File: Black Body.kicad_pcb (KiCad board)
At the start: 2 copper layers, 40 x 55.5 mm, 20 parts, among them IC2 MCP96L00T-E_MX, J1 53307-2471, J2 Conn_01x02, J3 Conn_01x03, J4 Conn_02x08_Top_Bottom

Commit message: Revision
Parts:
- added TP1: TestPoint, Connector_PinHeader_2.54mm:PinHeader_1x01_P2.54mm_Vertical, F.Cu at (125.6, 86.0)
- added TP2: TestPoint, Connector_PinHeader_2.54mm:PinHeader_1x01_P2.54mm_Vertical, F.Cu at (130.0, 86.0)
- added TP3: TestPoint, Connector_PinHeader_2.54mm:PinHeader_1x01_P2.54mm_Vertical, F.Cu at (134.2, 86.0)
- added TP4: TestPoint, Connector_PinHeader_2.54mm:PinHeader_1x01_P2.54mm_Vertical, F.Cu at (125.5, 91.5)
- added TP5: TestPoint, Connector_PinHeader_2.54mm:PinHeader_1x01_P2.54mm_Vertical, F.Cu at (130.2, 91.5)
- added TP6: TestPoint, Connector_PinHeader_2.54mm:PinHeader_1x01_P2.54mm_Vertical, F.Cu at (134.2, 91.5)
- added TP7: TestPoint, Connector_PinHeader_2.54mm:PinHeader_1x01_P2.54mm_Vertical, F.Cu at (125.2, 96.8)
- added TP8: TestPoint, Connector_PinHeader_2.54mm:PinHeader_1x01_P2.54mm_Vertical, F.Cu at (129.2, 96.8)
- C2, C3: footprint Capacitor_SMD:C_0603_1608Metric_Pad1.08x0.95mm_HandSolder -> Capacitor_SMD:C_0805_2012Metric_Pad1.18x1.45mm_HandSolder
- moved J2 0.50 mm to (109.5, 80.0)
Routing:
- net Net-(IC2-SCL): track 16.1 -> 30.1 mm, vias 1 -> 3
- net Net-(IC2-SDA): track 17.6 -> 30.6 mm, vias 1 -> 3
- net Net-(J1-ADC1_IN7): track 20.8 -> 32.7 mm
- net +3V3: track 31.4 -> 41.1 mm
- net GND: vias 3 -> 31
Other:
- board text added: "Kell wuz here"

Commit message: Updated Layout
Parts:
- removed D1, D2, D3, D4: 3V3, Diode_SMD:D_0603_1608Metric_Pad1.05x0.95mm_HandSolder
- removed TP1, TP2, TP3, TP4, TP5, TP6, TP7, TP8: TestPoint, Connector_PinHeader_2.54mm:PinHeader_1x01_P2.54mm_Vertical
- added DB_1: LED, LED_SMD:LED_0603_1608Metric_Pad1.05x0.95mm_HandSolder, F.Cu at (94.2, 94.2)
- added DB_2: LED, LED_SMD:LED_0603_1608Metric_Pad1.05x0.95mm_HandSolder, F.Cu at (98.5, 94.2)
- added DB_3: LED, LED_SMD:LED_0603_1608Metric_Pad1.05x0.95mm_HandSolder, F.Cu at (103.1, 94.2)
- added GND1: TestPoint, Connector_PinHeader_2.54mm:PinHeader_1x01_P2.54mm_Vertical, F.Cu at (119.0, 69.0)
- added GND2: TestPoint, Connector_PinHeader_2.54mm:PinHeader_1x01_P2.54mm_Vertical, F.Cu at (114.0, 69.0)
- added Heartbeat1: LED, LED_SMD:LED_0603_1608Metric_Pad1.05x0.95mm_HandSolder, F.Cu at (112.4, 105.5)
- added INT1: TestPoint, Connector_PinHeader_2.54mm:PinHeader_1x01_P2.54mm_Vertical, F.Cu at (120.2, 115.5)
- added IS_SCL1: TestPoint, Connector_PinHeader_2.54mm:PinHeader_1x01_P2.54mm_Vertical, F.Cu at (124.0, 110.8)
- added IS_SDA1: TestPoint, Connector_PinHeader_2.54mm:PinHeader_1x01_P2.54mm_Vertical, F.Cu at (119.8, 110.8)
- added J5: Conn_01x06, Connector_Molex:Molex_Nano-Fit_105313-xx06_1x06_P2.50mm_Horizontal, F.Cu at (131.9, 104.0)
- added R1: 10k, Resistor_SMD:R_0805_2012Metric, F.Cu at (121.6, 102.0)
- added R10: R, Resistor_SMD:R_0603_1608Metric_Pad0.98x0.95mm_HandSolder, F.Cu at (102.8, 92.2)
- added R2: 1.5k, Resistor_SMD:R_0805_2012Metric, F.Cu at (124.6, 102.0)
- added R3: 1.5k, Resistor_SMD:R_0805_2012Metric, F.Cu at (127.6, 101.9)
- added R9: R, Resistor_SMD:R_0603_1608Metric_Pad0.98x0.95mm_HandSolder, F.Cu at (118.5, 104.7)
- added TP_SCL1: LED, LED_SMD:LED_0603_1608Metric_Pad1.05x0.95mm_HandSolder, F.Cu at (118.6, 106.7)
- added TP_TC_1: TestPoint, Connector_PinHeader_2.54mm:PinHeader_1x01_P2.54mm_Vertical, F.Cu at (93.8, 109.5)
- added TP_TC_2: TestPoint, Connector_PinHeader_2.54mm:PinHeader_1x01_P2.54mm_Vertical, F.Cu at (93.8, 100.5)
- added TP_TC_F_1: TestPoint, Connector_PinHeader_2.54mm:PinHeader_1x01_P2.54mm_Vertical, F.Cu at (98.5, 109.2)
- added TP_TC_F_2: TestPoint, Connector_PinHeader_2.54mm:PinHeader_1x01_P2.54mm_Vertical, F.Cu at (98.8, 100.5)
- added VCC1: TestPoint, Connector_PinHeader_2.54mm:PinHeader_1x01_P2.54mm_Vertical, F.Cu at (115.5, 111.0)
- J3: value Conn_01x03 -> Conn_01x03_Pin
- J4: footprint MX150:CONN_SD-75900-001_2X08_MOL -> UTSVT_Connectors:CONN_SD-75900-001_2X08_MOL
- R4: value 1M -> R
- R7, R8: value 2M -> R
- moved J1 48.5 mm to (111.0, 117.0), turned to 0 degrees
- moved R6 33.5 mm to (97.8, 103.5)
- moved FB2 33.2 mm to (93.8, 103.5), turned to 0 degrees
- moved J2 32.4 mm to (89.5, 105.5)
- moved IC2 32.3 mm to (105.5, 106.5), turned to -90 degrees
- moved FB1 30.3 mm to (93.8, 105.5)
- moved C3 29.8 mm to (100.8, 104.5)
- moved Rb1 28.9 mm to (107.0, 99.8), turned to 0 degrees
- moved R5 28.5 mm to (97.8, 105.5), turned to 180 degrees
- moved J4 24.5 mm to (85.6, 84.2)
- moved Ra1 24.2 mm to (107.0, 97.8), turned to 180 degrees
- moved R4 23.3 mm to (94.3, 92.2), turned to 180 degrees
- moved C2 23.2 mm to (103.0, 98.8), turned to 90 degrees
- moved R7 21.7 mm to (98.4, 92.2)
- moved R8 16.8 mm to (112.4, 103.5)
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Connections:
- net Net-(J1-ADC1_IN7) renamed /INT
- C2 pad 1: +3V3 -> GND
- C2 pad 2: GND -> +3V3
- FB1 pad 2: Net-(D1-A) -> Net-(FB1-Pad2)
- FB2 pad 2: Net-(D2-A) -> Net-(FB2-Pad2)
- IC2 pad 11: unconnected-(IC2-ALERT_1-Pad11) -> /Alert_1
- IC2 pad 12: unconnected-(IC2-ALERT_2-Pad12) -> /Alert_2
- IC2 pad 14: unconnected-(IC2-ALERT_3-Pad14) -> /Alert_3
- IC2 pad 15: unconnected-(IC2-ALERT_4-Pad15) -> /Alert_4
- IC2 pad 19: Net-(IC2-SCL) -> /I2C1_SCL
- IC2 pad 20: Net-(IC2-SDA) -> /I2C1_SDA
- IC2 pad 8: +3V3 -> GND
- J1 pad 12: unconnected-(J1-SPI2_NSS-Pad12) -> /Alert_1
- J1 pad 14: unconnected-(J1-SPI2_MISO-Pad14) -> /Alert_4
- J1 pad 16: unconnected-(J1-SPI2_MOSI-Pad16) -> /Alert_3
- J1 pad 17: unconnected-(J1-SPI1_MOSI-Pad17) -> /DB_Conn_2
- J1 pad 18: unconnected-(J1-SPI2_SCK-Pad18) -> /Alert_2
- J1 pad 19: unconnected-(J1-SPI1_NSS-Pad19) -> /Heartbeat
- J1 pad 20: Net-(J1-CAN_L) -> /CAN_L
- J1 pad 21: unconnected-(J1-SPI1_MISO-Pad21) -> /DB_Conn_3
- J1 pad 22: Net-(J1-CAN_H) -> /CAN_H
- J1 pad 23: unconnected-(J1-SPI1_SCK-Pad23) -> /DB_Conn_1
- J1 pad 24: Net-(J1-+24V_In) -> +24V
- J1 pad 4: Net-(IC2-SDA) -> /I2C1_SDA
- J1 pad 6: Net-(IC2-SCL) -> /I2C1_SCL
- J3 pad 1: Net-(IC2-SCL) -> /I2C1_SDA
- J3 pad 2: Net-(IC2-SDA) -> /I2C1_SCL
- J4 pad 1: Net-(J1-+24V_In) -> +24V
- J4 pad 12: unconnected-(J4-Pin_12-Pad12) -> /CAN_L
- J4 pad 13: unconnected-(J4-Pin_13-Pad13) -> /CAN_H
- J4 pad 5: Net-(J1-CAN_H) -> /CAN_H
- J4 pad 6: Net-(J1-CAN_L) -> /CAN_L
- J4 pad 8: unconnected-(J4-Pin_8-Pad8) -> GND
- J4 pad 9: unconnected-(J4-Pin_9-Pad9) -> +24V
- R4 pad 1: Net-(D2-A) -> Net-(DB_1-A)
- R5 pad 2: Net-(D1-A) -> Net-(FB1-Pad2)
- R6 pad 2: Net-(D2-A) -> Net-(FB2-Pad2)
- R7 pad 1: GND -> Net-(DB_2-A)
- R7 pad 2: Net-(D1-A) -> +3V3
- R8 pad 1: GND -> Net-(Heartbeat1-A)
- R8 pad 2: Net-(D2-A) -> +3V3
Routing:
- net /I2C1_SCL: track 0.00 -> 80.2 mm, vias 0 -> 1
- net /I2C1_SDA: track 0.00 -> 68.2 mm, vias 0 -> 2
- net /CAN_L: track 0.00 -> 53.4 mm, vias 0 -> 3
- net /CAN_H: track 0.00 -> 48.0 mm, vias 0 -> 3
- net +3V3: track 41.1 -> 3.10 mm, vias 3 -> 0
- net Net-(J1-CAN_L): track 33.8 -> 0.00 mm
- net /DB_Conn_1: track 0.00 -> 30.7 mm, vias 0 -> 1
- net /DB_Conn_2: track 0.00 -> 30.7 mm, vias 0 -> 3
- net Net-(IC2-SDA): track 30.6 -> 0.00 mm, vias 3 -> 0
- net Net-(IC2-SCL): track 30.1 -> 0.00 mm, vias 3 -> 0
- net Net-(J1-CAN_H): track 29.6 -> 0.00 mm, vias 1 -> 0
- net Net-(D2-A): track 29.5 -> 0.00 mm, vias 3 -> 0
- net /INT: track 32.7 -> 60.5 mm, vias 0 -> 2
- net /DB_Conn_3: track 0.00 -> 27.4 mm, vias 0 -> 1
- net Net-(J1-+24V_In): track 24.1 -> 0.00 mm, vias 2 -> 0
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- added copper zone on F.Cu, net +24V
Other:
- board outline removed
- board text removed: "Kell wuz here"

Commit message: connector update
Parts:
- moved GND1 23.8 mm to (113.8, 92.2)
- moved GND2 23.8 mm to (108.8, 92.2)
- moved INT1 2.75 mm to (120.2, 118.2)
- moved TP_TC_F_2 0.75 mm to (98.8, 99.8)
- moved TP_TC_2 0.40 mm to (93.5, 100.2)
- moved J2 0.31 mm to (89.1, 105.5)
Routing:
- net +3V3: track 3.10 -> 71.9 mm, vias 0 -> 3
- net +24V: track 0.00 -> 38.6 mm, vias 0 -> 2
- net /I2C1_SCL: track 80.2 -> 75.8 mm, vias 1 -> 2
- net /INT: track 60.5 -> 62.6 mm
- net Net-(J2-Pin_2): track 7.05 -> 8.41 mm
- net Net-(IC2-VIN+): track 11.6 -> 12.4 mm
- net /DB_Conn_2: vias 3 -> 4
- removed copper zone on F.Cu, net +24V
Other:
- board outline added: 78.8 x 58 mm
- board text added: "Kell wuz here"
- board text added: "and Issac and Tanya"

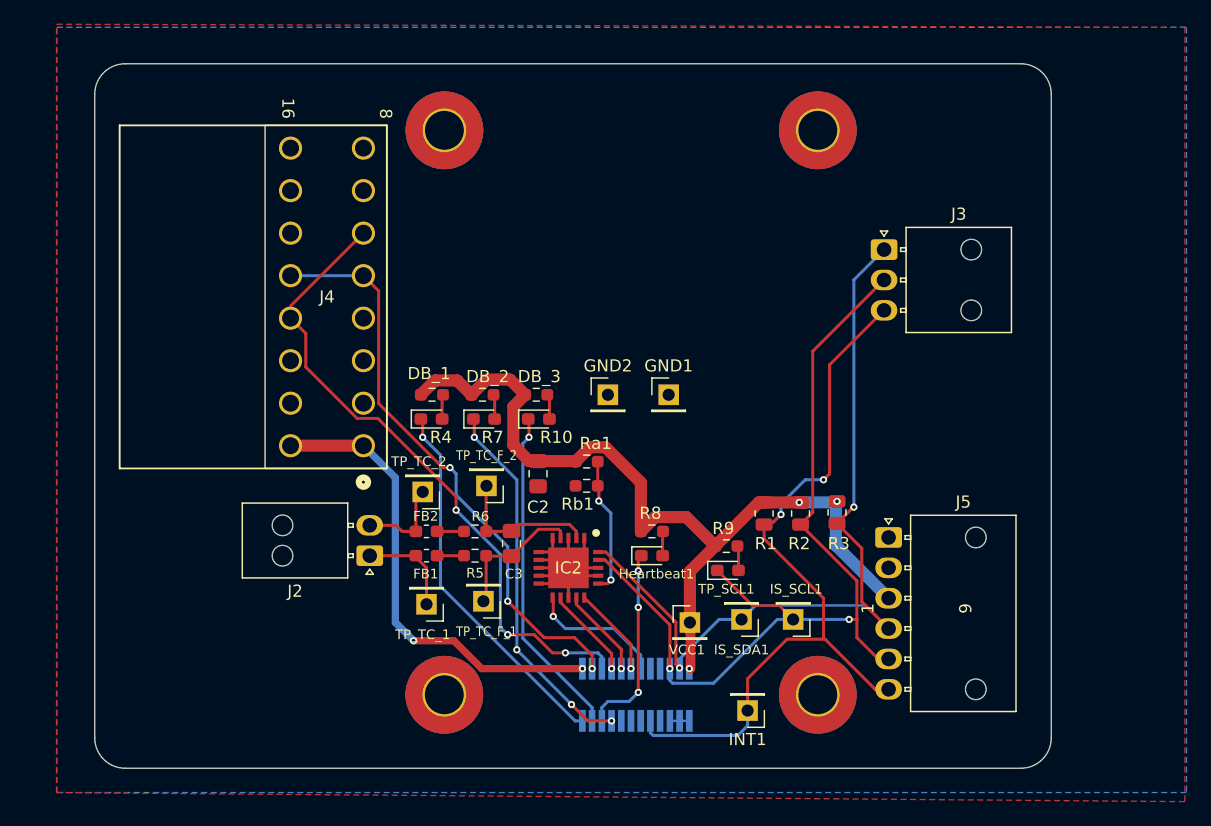
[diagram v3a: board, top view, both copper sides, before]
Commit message: updated layout
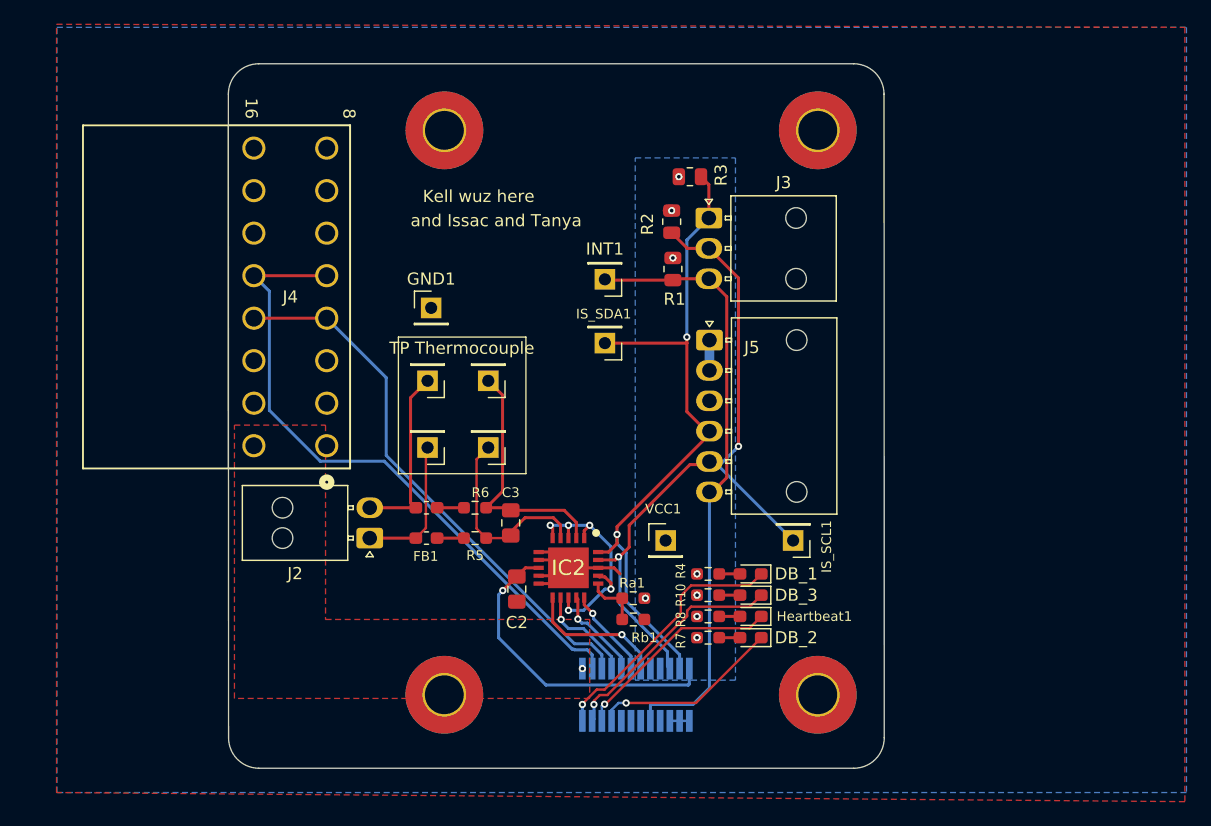
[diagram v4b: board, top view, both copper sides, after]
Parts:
- removed GND2: TestPoint, Connector_PinHeader_2.54mm:PinHeader_1x01_P2.54mm_Vertical
- removed R9: R, Resistor_SMD:R_0603_1608Metric_Pad0.98x0.95mm_HandSolder
- removed TP_SCL1: LED, LED_SMD:LED_0603_1608Metric_Pad1.05x0.95mm_HandSolder
- R10, R4, R7, R8: value R -> 1k
- moved INT1 37.4 mm to (108.5, 82.8)
- moved R3 30.2 mm to (115.5, 74.3), turned to 0 degrees
- moved DB_1 29.2 mm to (120.5, 107.0), turned to 180 degrees
- moved DB_2 28.4 mm to (120.5, 112.2), turned to 180 degrees
- moved R7 27.3 mm to (117.0, 112.2)
- moved R4 27.1 mm to (117.0, 107.0)
- moved R2 26.3 mm to (114.0, 78.0)
- moved IS_SDA1 25.4 mm to (108.5, 88.0)
- moved DB_3 22.7 mm to (120.5, 108.8), turned to 180 degrees
- moved J5 21.9 mm to (117.1, 87.8)
- moved R10 21.7 mm to (117.0, 108.8)
- moved R1 21.5 mm to (114.1, 81.9)
- moved GND1 20.8 mm to (94.2, 85.1)
- moved J3 14.7 mm to (117.1, 77.7)
- moved TP_TC_1 12.9 mm to (93.9, 96.6)
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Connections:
- IC2 pad 1: GND -> SYS_GND
- IC2 pad 13: GND -> SYS_GND
- IC2 pad 17: GND -> SYS_GND
- IC2 pad 3: GND -> SYS_GND
- IC2 pad 5: GND -> SYS_GND
- IC2 pad 8: GND -> +3V3
- J4 pad 4: unconnected-(J4-Pin_4-Pad4) -> /CAN_L
- J4 pad 6: /CAN_L -> unconnected-(J4-Pin_6-Pad6)
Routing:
- net +3V3: track 71.9 -> 26.6 mm, vias 3 -> 9
- net +24V: track 38.6 -> 0.00 mm, vias 2 -> 1
- net SYS_GND: track 0.00 -> 19.7 mm, vias 0 -> 5
- net /I2C1_SCL: track 75.8 -> 58.5 mm
- net /DB_Conn_2: track 30.7 -> 15.7 mm, vias 4 -> 1
- net /INT: track 62.6 -> 50.5 mm, vias 2 -> 0
- net /I2C1_SDA: track 68.2 -> 56.9 mm
- net /DB_Conn_1: track 30.7 -> 21.4 mm
- net /CAN_L: track 53.4 -> 45.0 mm, vias 3 -> 0
- net Net-(IC2-VIN+): track 12.4 -> 20.7 mm
- net /DB_Conn_3: track 27.4 -> 19.4 mm
- net GND: track 29.7 -> 22.7 mm
- net Net-(IC2-ADDR): track 11.4 -> 4.84 mm, vias 2 -> 0
- net Net-(J2-Pin_2): track 8.41 -> 14.7 mm
- net /CAN_H: track 48.0 -> 53.7 mm, vias 3 -> 0
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- added copper zone on F.Cu, net +24V
- added copper zone on B.Cu, net +3V3
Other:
- board size 78.8 x 58 mm -> 54 x 58 mm
- board text added: "TP Thermocouple"

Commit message: updated bb
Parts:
- added F1: 0.5, Fuse:Fuse_0603_1608Metric_Pad1.05x0.95mm_HandSolder, F.Cu at (89.0, 95.2)
- added G***: LOGO, LOGO, F.Cu at (97.5, 80.5)
- added R11: 1.5k, Resistor_SMD:R_0805_2012Metric, F.Cu at (113.1, 103.3)
- added R12: 1.5k, Resistor_SMD:R_0805_2012Metric, F.Cu at (113.1, 106.2)
- added R9: 0, Resistor_SMD:R_0603_1608Metric_Pad0.98x0.95mm_HandSolder, F.Cu at (108.2, 101.2)
- GND: renamed from GND1; footprint Connector_PinHeader_2.54mm:PinHeader_1x01_P2.54mm_Vertical -> TestPoint:TestPoint_Pad_1.0x1.0mm
- J3: value Conn_01x03_Pin -> Conn_01x04; footprint Connector_Molex:Molex_Nano-Fit_105313-xx03_1x03_P2.50mm_Horizontal -> Connector_PinHeader_2.54mm:PinHeader_1x04_P2.54mm_Horizontal
- TP_TC_1, TP_TC_2, TP_TC_F_1, TP_TC_F_2: footprint Connector_PinHeader_2.54mm:PinHeader_1x01_P2.54mm_Vertical -> TestPoint:TestPoint_Pad_1.0x1.0mm
- VCC: renamed from VCC1; footprint Connector_PinHeader_2.54mm:PinHeader_1x01_P2.54mm_Vertical -> TestPoint:TestPoint_Pad_1.0x1.0mm
- moved GND 14.0 mm to (108.0, 83.0)
- moved VCC 8.50 mm to (113.2, 95.8)
- moved R3 7.04 mm to (113.3, 81.0)
- moved INT1 6.81 mm to (108.4, 75.9)
- moved R1 6.81 mm to (114.0, 75.1)
- moved J3 1.79 mm to (117.4, 75.9)
- moved R2 0.90 mm to (113.2, 78.5), turned to 0 degrees
- moved I2C_SCL 0.25 mm to (124.0, 104.5)
- renumbered IS_SCL1 to I2C_SCL, IS_SDA1 to I2C_SDA
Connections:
- J3 pad 1: /I2C1_SDA -> /INT
- J3 pad 3: /INT -> /I2C1_SDA
- J4 pad 9: +24V -> Net-(J4-Pin_9)
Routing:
- net +3V3: track 26.6 -> 76.5 mm, vias 9 -> 10
- net /I2C1_SDA: track 56.9 -> 70.4 mm
- net Net-(J4-Pin_9): track 0.00 -> 10.3 mm
- net /INT: track 50.5 -> 59.0 mm
- net /CAN_H: track 53.7 -> 48.5 mm, vias 0 -> 1
- net /I2C1_SCL: track 58.5 -> 62.0 mm
- net SYS_GND: track 19.7 -> 21.5 mm
- net GND: track 22.7 -> 21.1 mm, vias 0 -> 27
- net +24V: vias 1 -> 29
- added copper zone on B.Cu, net +24V
- removed copper zone on F.Cu, net +24V
- removed copper zone on B.Cu, net +3V3
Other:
- board size 54 x 58 mm -> 52 x 53.5 mm
- board text added: "Filter 1"
- board text added: "Filter 2"
- board text added: "GND"
- board text added: "INT"
- board text added: "IS SCL"
- board text added: "IS SDA"
- board text added: "TC 1"
- board text added: "TC 2"
- board text added: "and Isaac and Tanya"
- board text removed: "and Issac and Tanya"
